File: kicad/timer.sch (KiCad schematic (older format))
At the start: 1 part

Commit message: Initial footprint
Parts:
- added IC1: ATMEGA328P-A, Housings_QFP:TQFP-32_7x7mm_Pitch0.8mm, symbol ATMEGA328P-A
- added U1: TOUCH_PAD_15, touch_timer:touch_pad_rect, symbol TOUCH_PAD_15
- U2: renamed from U?; footprint (none) -> Housings_SSOP:SSOP-28_5.3x10.2mm_Pitch0.65mm
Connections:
- net labels added: INT, RX0, RX1, RX10, RX11, RX12, RX13, RX14, RX2, RX3, RX4, RX5, RX6, RX7, RX8, RX9, SCL, SDA
- wire segments 0 -> 21
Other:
- moved on the sheet: U2
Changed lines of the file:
@@
 $EndDescr
 $Comp
-L MTCH6102_SSOP U?
+L MTCH6102_SSOP U2
 U 1 1 570281AD
-P 5550 2900
-F 0 "U?" H 5550 3300 60  0000 C CNN
-F 1 "MTCH6102_SSOP" H 5550 3150 60  0000 C CNN
-F 2 "" H 5550 2900 60  0000 C CNN
-F 3 "" H 5550 2900 60  0000 C CNN
-	1    5550 2900
+P 5200 2400
+F 0 "U2" H 5200 2800 60  0000 C CNN
+F 1 "MTCH6102_SSOP" H 5200 2650 60  0000 C CNN
+F 2 "Housings_SSOP:SSOP-28_5.3x10.2mm_Pitch0.65mm" H 5200 2400 60  0001 C CNN
+F 3 "" H 5200 2400 60  0000 C CNN
+	1    5200 2400
 	1    0    0    -1
 $EndComp
+$Comp
+L ATMEGA328P-A IC1
+U 1 1 5703AB3B
+P 8300 3250
+F 0 "IC1" H 7550 4500 50  0000 L BNN
+F 1 "ATMEGA328P-A" H 8700 1850 50  0000 L BNN
+F 2 "Housings_QFP:TQFP-32_7x7mm_Pitch0.8mm" H 8300 3250 50  0000 C CIN
+F 3 "" H 8300 3250 50  0000 C CNN
+	1    8300 3250
+	-1   0    0    -1
+$EndComp
+Text Label 6950 3400 0    60   ~ 0
+SDA
+Text Label 6950 3500 0    60   ~ 0
+SCL
+Text Label 6950 3950 0    60   ~ 0
+INT
+Text Label 6100 2600 0    60   ~ 0
+SDA
+Text Label 6100 2700 0    60   ~ 0
+SCL
+Text Label 6100 2800 0    60   ~ 0
+INT
+Wire Wire Line
+	7300 3400 6950 3400
+Wire Wire Line
+	7300 3500 6950 3500
+Wire Wire Line
+	7300 3950 6950 3950
+Wire Wire Line
+	5750 2600 6100 2600
+Wire Wire Line
+	5750 2700 6100 2700
+Wire Wire Line
+	5750 2800 6100 2800
+$Comp
+L TOUCH_PAD_15 U1
+U 1 1 5703B32D
+P 3350 2500
+F 0 "U1" H 3350 750 60  0000 C CNN
+F 1 "TOUCH_PAD_15" H 3350 2600 60  0000 C CNN
+F 2 "touch_timer:touch_pad_rect" H 3350 2500 60  0001 C CNN
+F 3 "" H 3350 2500 60  0000 C CNN
+	1    3350 2500
+	1    0    0    -1
+$EndComp
+Wire Wire Line
+	3900 2700 4650 2700
+Wire Wire Line
+	3900 2800 4650 2800
+Wire Wire Line
+	3900 2900 4650 2900
+Wire Wire Line
+	3900 3000 4650 3000
+Wire Wire Line
+	3900 3100 4650 3100
+Wire Wire Line
+	3900 3200 4650 3200
+Wire Wire Line
+	3900 3300 4650 3300
+Wire Wire Line
+	3900 3400 4650 3400
+Wire Wire Line
+	3900 3500 4650 3500
+Wire Wire Line
+	3900 3600 4650 3600
+Wire Wire Line
+	3900 3700 4650 3700
+Wire Wire Line
+	3900 3800 4650 3800
+Wire Wire Line
+	3900 3900 4650 3900
+Wire Wire Line
+	3900 4000 4650 4000
+Wire Wire Line
+	3900 4100 4650 4100
+Text Label 4400 2700 0    60   ~ 0
+RX0
+Text Label 4400 2800 0    60   ~ 0
+RX1
+Text Label 4400 2900 0    60   ~ 0
+RX2
+Text Label 4400 3000 0    60   ~ 0
+RX3
+Text Label 4400 3100 0    60   ~ 0
+RX4
+Text Label 4400 3200 0    60   ~ 0
+RX5
+Text Label 4400 3300 0    60   ~ 0
+RX6
+Text Label 4400 3400 0    60   ~ 0
+RX7
+Text Label 4400 3500 0    60   ~ 0
+RX8
+Text Label 4400 3600 0    60   ~ 0
+RX9
+Text Label 4400 3700 0    60   ~ 0
+RX10
+Text Label 4400 3800 0    60   ~ 0
+RX11
+Text Label 4400 3900 0    60   ~ 0
+RX12
+Text Label 4400 4000 0    60   ~ 0
+RX13
+Text Label 4400 4100 0    60   ~ 0
+RX14
 $EndSCHEMATC

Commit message: Clock like input
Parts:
- removed U1: TOUCH_PAD_15, touch_timer:touch_pad_rect, symbol TOUCH_PAD_15
- added U1: TOUCH_PAD_13, touch_timer:touch_circle, symbol TOUCH_PAD_13
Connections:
- net labels removed: RX13, RX14
- wire segments 21 -> 19
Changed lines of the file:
@@
 Wire Wire Line
 	5750 2800 6100 2800
-$Comp
-L TOUCH_PAD_15 U1
-U 1 1 5703B32D
-P 3350 2500
-F 0 "U1" H 3350 750 60  0000 C CNN
-F 1 "TOUCH_PAD_15" H 3350 2600 60  0000 C CNN
-F 2 "touch_timer:touch_pad_rect" H 3350 2500 60  0001 C CNN
-F 3 "" H 3350 2500 60  0000 C CNN
-	1    3350 2500
-	1    0    0    -1
-$EndComp
 Wire Wire Line
 	3900 2700 4650 2700
@@
 Wire Wire Line
 	3900 3900 4650 3900
-Wire Wire Line
-	3900 4000 4650 4000
-Wire Wire Line
-	3900 4100 4650 4100
 Text Label 4400 2700 0    60   ~ 0
 RX0
@@
 Text Label 4400 3900 0    60   ~ 0
 RX12
-Text Label 4400 4000 0    60   ~ 0
-RX13
-Text Label 4400 4100 0    60   ~ 0
-RX14
+$Comp
+L TOUCH_PAD_13 U1
+U 1 1 5704144A
+P 3350 2500
+F 0 "U1" H 3350 750 60  0000 C CNN
+F 1 "TOUCH_PAD_13" H 3350 2600 60  0000 C CNN
+F 2 "touch_timer:touch_circle" H 3350 2500 60  0001 C CNN
+F 3 "" H 3350 2500 60  0000 C CNN
+	1    3350 2500
+	1    0    0    -1
+$EndComp
 $EndSCHEMATC

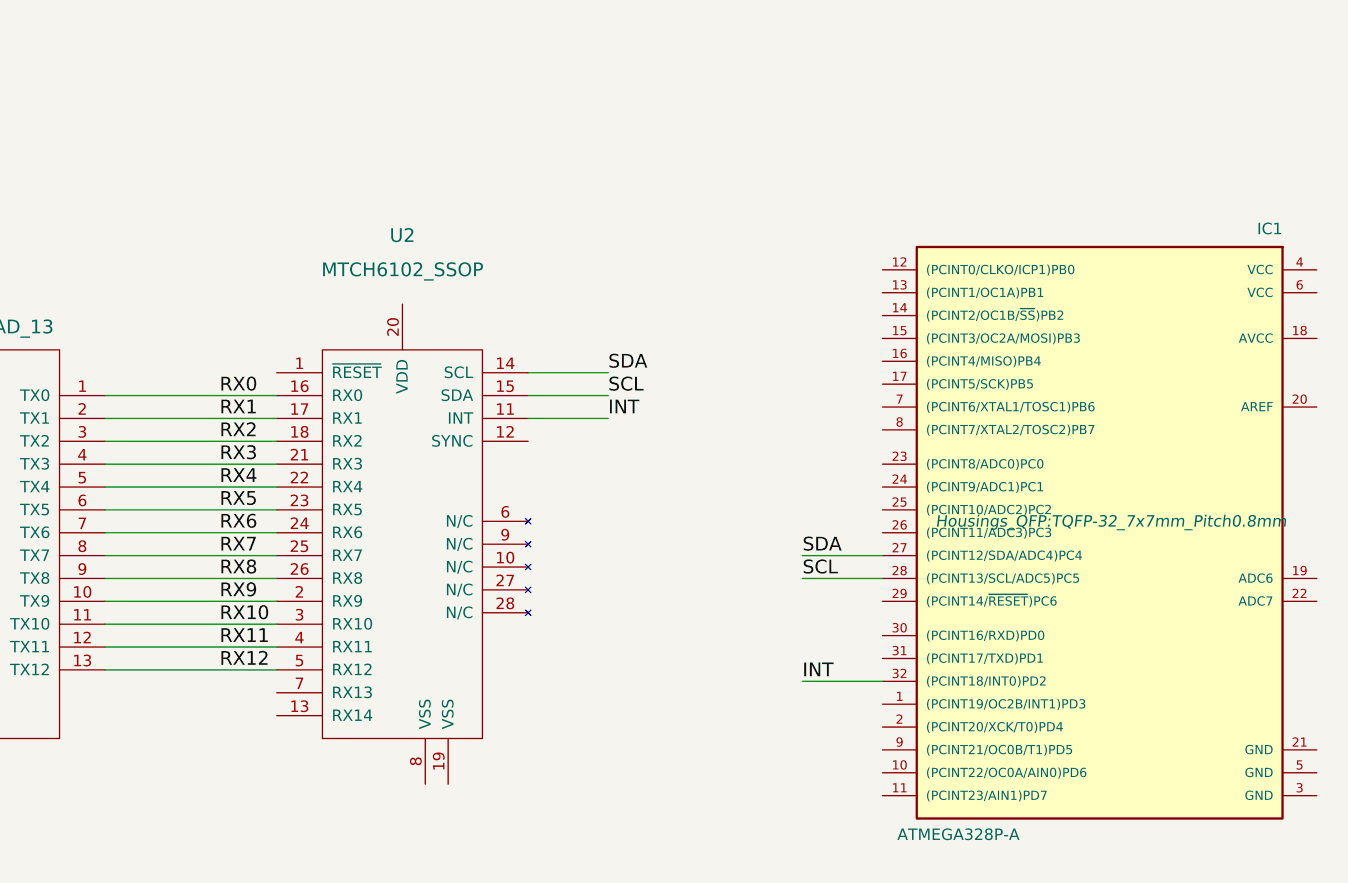
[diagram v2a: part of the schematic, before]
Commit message: Caps & resistors on the touch ic
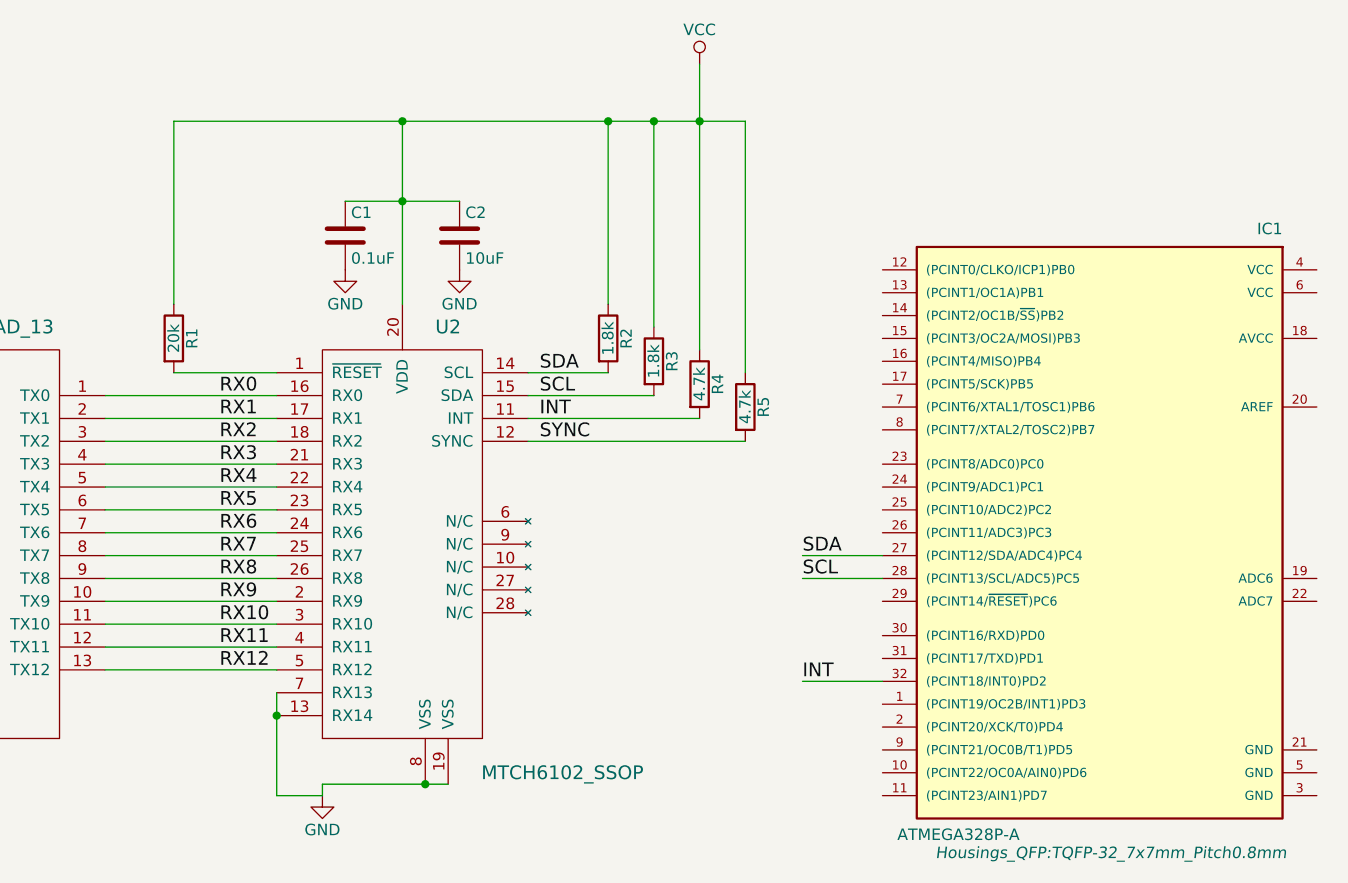
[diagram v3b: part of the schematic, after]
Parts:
- added C1: 0.1uF, Capacitors_SMD:C_0805_HandSoldering, symbol C
- added C2: 10uF, Capacitors_SMD:C_0805_HandSoldering, symbol C
- added R1: 20k, Resistors_SMD:R_0805_HandSoldering, symbol R
- added R2, R3: 1.8k, Resistors_SMD:R_0805_HandSoldering, symbol R
- added R4, R5: 4.7k, Resistors_SMD:R_0805_HandSoldering, symbol R
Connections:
- net INT: now also R4.2
- net SCL: now also R3.2
- net SDA: now also R2.2
- net at U2.1 (~RESET): now also R1.2
- net SYNC: now reaches U2.12 (SYNC)
- net SYNC: now also R5.2
- net GND: now reaches U2.13 (RX14)
- net GND: now also U2.19 (VSS), U2.7 (RX13), U2.8 (VSS), C1.2, C2.2
- net VCC: now reaches U2.20 (VDD)
- net VCC: now also C1.1, C2.1, R1.1, R2.1, R3.1, R4.1, R5.1
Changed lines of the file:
@@
 U 1 1 570281AD
 P 5200 2400
-F 0 "U2" H 5200 2800 60  0000 C CNN
-F 1 "MTCH6102_SSOP" H 5200 2650 60  0000 C CNN
+F 0 "U2" H 5400 2400 60  0000 C CNN
+F 1 "MTCH6102_SSOP" H 5900 450 60  0000 C CNN
 F 2 "Housings_SSOP:SSOP-28_5.3x10.2mm_Pitch0.65mm" H 5200 2400 60  0001 C CNN
 F 3 "" H 5200 2400 60  0000 C CNN
@@
 F 0 "IC1" H 7550 4500 50  0000 L BNN
 F 1 "ATMEGA328P-A" H 8700 1850 50  0000 L BNN
-F 2 "Housings_QFP:TQFP-32_7x7mm_Pitch0.8mm" H 8300 3250 50  0000 C CIN
+F 2 "Housings_QFP:TQFP-32_7x7mm_Pitch0.8mm" H 8300 1800 50  0000 C CIN
 F 3 "" H 8300 3250 50  0000 C CNN
 	1    8300 3250
@@
 Text Label 6950 3950 0    60   ~ 0
 INT
-Text Label 6100 2600 0    60   ~ 0
+Text Label 5800 2600 0    60   ~ 0
 SDA
-Text Label 6100 2700 0    60   ~ 0
+Text Label 5800 2700 0    60   ~ 0
 SCL
-Text Label 6100 2800 0    60   ~ 0
+Text Label 5800 2800 0    60   ~ 0
 INT
 Wire Wire Line
@@
 	5750 2600 6100 2600
 Wire Wire Line
-	5750 2700 6100 2700
-Wire Wire Line
-	5750 2800 6100 2800
+	5750 2700 6300 2700
+Wire Wire Line
+	5750 2800 6500 2800
 Wire Wire Line
 	3900 2700 4650 2700
@@
 	1    0    0    -1
 $EndComp
+$Comp
+L R R2
+U 1 1 5704F448
+P 6100 2450
+F 0 "R2" V 6180 2450 50  0000 C CNN
+F 1 "1.8k" V 6100 2450 50  0000 C CNN
+F 2 "Resistors_SMD:R_0805_HandSoldering" V 6030 2450 50  0001 C CNN
+F 3 "" H 6100 2450 50  0000 C CNN
+	1    6100 2450
+	1    0    0    -1
+$EndComp
+$Comp
+L R R3
+U 1 1 5704F490
+P 6300 2550
+F 0 "R3" V 6380 2550 50  0000 C CNN
+F 1 "1.8k" V 6300 2550 50  0000 C CNN
+F 2 "Resistors_SMD:R_0805_HandSoldering" V 6230 2550 50  0001 C CNN
+F 3 "" H 6300 2550 50  0000 C CNN
+	1    6300 2550
+	1    0    0    -1
+$EndComp
+$Comp
+L R R4
+U 1 1 5704F5FC
+P 6500 2650
+F 0 "R4" V 6580 2650 50  0000 C CNN
+F 1 "4.7k" V 6500 2650 50  0000 C CNN
+F 2 "Resistors_SMD:R_0805_HandSoldering" V 6430 2650 50  0001 C CNN
+F 3 "" H 6500 2650 50  0000 C CNN
+	1    6500 2650
+	1    0    0    -1
+$EndComp
+$Comp
+L R R5
+U 1 1 5704F67F
+P 6700 2750
+F 0 "R5" V 6780 2750 50  0000 C CNN
+F 1 "4.7k" V 6700 2750 50  0000 C CNN
+F 2 "Resistors_SMD:R_0805_HandSoldering" V 6630 2750 50  0001 C CNN
+F 3 "" H 6700 2750 50  0000 C CNN
+	1    6700 2750
+	1    0    0    -1
+$EndComp
+Wire Wire Line
+	5750 2900 6700 2900
+$Comp
+L VCC #PWR01
+U 1 1 5704F74C
+P 6500 1250
+F 0 "#PWR01" H 6500 1100 50  0001 C CNN
+F 1 "VCC" H 6500 1400 50  0000 C CNN
+F 2 "" H 6500 1250 50  0000 C CNN
+F 3 "" H 6500 1250 50  0000 C CNN
+	1    6500 1250
+	1    0    0    -1
+$EndComp
+Wire Wire Line
+	6100 2300 6100 1500
+Wire Wire Line
+	4200 1500 6700 1500
+Wire Wire Line
+	6500 1250 6500 2500
+Wire Wire Line
+	6300 2400 6300 1500
+Connection ~ 6300 1500
+Connection ~ 6500 1500
+Wire Wire Line
+	6700 1500 6700 2600
+Text Label 5800 2900 0    60   ~ 0
+SYNC
+$Comp
+L R R1
+U 1 1 5704F972
+P 4200 2450
+F 0 "R1" V 4280 2450 50  0000 C CNN
+F 1 "20k" V 4200 2450 50  0000 C CNN
+F 2 "Resistors_SMD:R_0805_HandSoldering" V 4130 2450 50  0001 C CNN
+F 3 "" H 4200 2450 50  0000 C CNN
+	1    4200 2450
+	1    0    0    -1
+$EndComp
+Wire Wire Line
+	4650 2600 4200 2600
+Wire Wire Line
+	4200 2300 4200 1500
+Connection ~ 6100 1500
+Wire Wire Line
+	5200 2300 5200 1500
+Connection ~ 5200 1500
+$Comp
+L C C1
+U 1 1 5704FB03
+P 4950 2000
+F 0 "C1" H 4975 2100 50  0000 L CNN
+F 1 "0.1uF" H 4975 1900 50  0000 L CNN
+F 2 "Capacitors_SMD:C_0805_HandSoldering" H 4988 1850 50  0001 C CNN
+F 3 "" H 4950 2000 50  0000 C CNN
+	1    4950 2000
+	1    0    0    -1
+$EndComp
+$Comp
+L C C2
+U 1 1 5704FB99
+P 5450 2000
+F 0 "C2" H 5475 2100 50  0000 L CNN
+F 1 "10uF" H 5475 1900 50  0000 L CNN
+F 2 "Capacitors_SMD:C_0805_HandSoldering" H 5488 1850 50  0001 C CNN
+F 3 "" H 5450 2000 50  0000 C CNN
+	1    5450 2000
+	1    0    0    -1
+$EndComp
+Wire Wire Line
+	4950 1850 5450 1850
+Connection ~ 5200 1850
+$Comp
+L GND #PWR02
+U 1 1 5704FD9B
+P 4950 2150
+F 0 "#PWR02" H 4950 1900 50  0001 C CNN
+F 1 "GND" H 4950 2000 50  0000 C CNN
+F 2 "" H 4950 2150 50  0000 C CNN
+F 3 "" H 4950 2150 50  0000 C CNN
+	1    4950 2150
+	1    0    0    -1
+$EndComp
+$Comp
+L GND #PWR03
+U 1 1 5704FDE9
+P 5450 2150
+F 0 "#PWR03" H 5450 1900 50  0001 C CNN
+F 1 "GND" H 5450 2000 50  0000 C CNN
+F 2 "" H 5450 2150 50  0000 C CNN
+F 3 "" H 5450 2150 50  0000 C CNN
+	1    5450 2150
+	1    0    0    -1
+$EndComp
+$Comp
+L GND #PWR04
+U 1 1 5704FF0B
+P 4850 4450
+F 0 "#PWR04" H 4850 4200 50  0001 C CNN
+F 1 "GND" H 4850 4300 50  0000 C CNN
+F 2 "" H 4850 4450 50  0000 C CNN
+F 3 "" H 4850 4450 50  0000 C CNN
+	1    4850 4450
+	1    0    0    -1
+$EndComp
+Wire Wire Line
+	4650 4000 4650 4450
+Wire Wire Line
+	4650 4450 4850 4450
+Connection ~ 4650 4100
+Wire Wire Line
+	4850 4400 5400 4400
+Wire Wire Line
+	4850 4450 4850 4400
+Connection ~ 5300 4400
 $EndSCHEMATC

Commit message: Sqeeze it in
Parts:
- added C3, C4: 1uF, Capacitors_SMD:C_0805_HandSoldering, symbol C
- added C5: 0.1uF, Capacitors_SMD:C_0805_HandSoldering, symbol C
- added D1: D_Schottky, Diodes_SMD:SOD-123, symbol D_Schottky
- added D2: Led, LEDs:LED_0805, symbol Led_Small
- added P1: BATTERY, Pin_Headers:Pin_Header_Straight_1x02, symbol CONN_01X02
- added P2: ICSP, Pin_Headers:Pin_Header_Straight_2x03, symbol CONN_02X03
- added Q1: NMOS, TO_SOT_Packages_SMD:SOT-23_Handsoldering, symbol Q_NMOS_GSD
- added Q2: PMOS, TO_SOT_Packages_SMD:SOT-23_Handsoldering, symbol Q_PMOS_GSD
- added R10: 100k, Resistors_SMD:R_0805_HandSoldering, symbol R
- added R6: 220, Resistors_SMD:R_0805_HandSoldering, symbol R
- added R7: 10K, Resistors_SMD:R_0805_HandSoldering, symbol R
- added R8: 100K, Resistors_SMD:R_0805_HandSoldering, symbol R
- added R9: 820, Resistors_SMD:R_0805_HandSoldering, symbol R
- added SW1: SPST, SMD_Packages:SMD-2010_Pol, symbol SPST
- added U3: MCP1755ST-3302E/DB, TO_SOT_Packages_SMD:SOT-223, symbol MCP1755ST-3302E/DB
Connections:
- net GND: now also IC1.21 (GND), IC1.3 (GND), IC1.5 (GND), C3.2, C4.2, C5.2, D2.1 (K), P1.1 (P1), P2.6 (P6), Q1.2 (S), R10.2, R7.2, U3.2 (GND), U3.4 (GND)
- net VCC: now also P1.2 (P2), SW1.2; no longer C1.1, C2.1, R1.1, R2.1, R3.1, R4.1, R5.1, U2.20 (VDD)
- net NBASE_ON: now reaches IC1.13 ((PCINT1/OC1A)PB1)
- net NBASE_ON: now also R6.2
- net MOSI: now reaches IC1.15 ((PCINT3/OC2A/MOSI)PB3)
- net MOSI: now also P2.4 (P4)
- net MISO: now reaches IC1.16 ((PCINT4/MISO)PB4)
- net MISO: now also P2.1 (P1)
- net SCK: now reaches IC1.17 ((PCINT5/SCK)PB5)
- net SCK: now also P2.3 (P3), R9.1
- net RESET: now reaches IC1.29 ((PCINT14/~RESET~)PC6)
- net RESET: now also P2.5 (P5), R10.1
- net 3V3: now reaches IC1.4 (VCC)
- net 3V3: now also C1.1, C2.1, IC1.6 (VCC), R1.1, R2.1, R3.1, R5.1, U2.20 (VDD), C4.1, C5.1, U3.3 (VO)
- new net: D1.2 (A), SW1.1
- new net: D2.2 (A), R9.2
- new net NBASE: Q1.1 (G), R6.1, R7.1
- new net PBASE: Q1.3 (D), Q2.1 (G), R8.2
- new net POWER: D1.1 (K), Q2.3 (D), R8.1
- new net SWITCHED_POWER: C3.1, P2.2 (P2), Q2.2 (S), U3.1 (VI)
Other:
- moved on the sheet: C1, C2, IC1, R1, R2, R3, R4, R5, U1, U2
